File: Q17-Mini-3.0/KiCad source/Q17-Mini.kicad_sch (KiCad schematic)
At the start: 80 parts, among them J1 INPUT, J2-1 SPK+, J2-2 SPK-, J3-1 V+, J3-2 GND, J3-3 V-, Q1 IRF610, Q10 KSA992, Q12 KSC1845, Q13 IRF610, Q14 IRF9610, Q15 FQA46N15, Q16 IXTH48P20P, Q2 KSA992, Q3 KSC1845, Q4 IRF9610, Q5 FQPF7P20, Q6 2SK3564, Q7 LSK170B, Q8 DN2540, Q9 BS250P, U1 OPA1611, U2 NDC7003P

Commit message: Update Q17-Mini.kicad_sch
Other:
- note added: "105mA"
- note added: "95mA"
- note added: "Board consumption per voltage rail without power transistors: 10mA"
- note removed: "35mV with R32 = 10R"
- note removed: "If you have ground loop concerns, you can put R32=0R on one board and R32=10R on the second board. This fixes the problem."
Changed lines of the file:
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@@
 	(title_block
 		(title "Q17-Mini Amplifier")
-		(date "2024-06-29")
-		(rev "2.3.1")
+		(date "2024-07-02")
+		(rev "2.3.2")
 		(company "Principe circuit by Tiberiu Vicol")
 		(comment 1 "Modified by Stef for the Q17-Mini project")
@@
 	(text "max 55V"
 		(exclude_from_sim no)
-		(at 269.24 71.12 0)
+		(at 269.494 68.072 0)
 		(effects
 			(font
@@
 		)
 	)
-	(text "If you have ground loop concerns, you can put R32=0R on one board and R32=10R on the second board. This fixes the problem."
+	(text "Board consumption per voltage rail without power transistors: 10mA"
 		(exclude_from_sim no)
-		(at 85.09 15.24 0)
+		(at 121.412 15.24 0)
 		(effects
 			(font
@@
 		)
 	)
-	(text "35mV with R32 = 10R"
-		(exclude_from_sim no)
-		(at 196.088 81.28 0)
-		(effects
-			(font
-				(size 1.27 1.27)
-				(color 255 3 20 1)
-			)
-			(justify left bottom)
-		)
-	)
 	(text "Q9, U2 : Wilson current mirror (CCS)"
 		(exclude_from_sim no)
@@
 		)
 	)
+	(text "105mA"
+		(exclude_from_sim no)
+		(at 255.27 139.954 0)
+		(effects
+			(font
+				(size 1.27 1.27)
+			)
+			(justify left bottom)
+		)
+	)
 	(text "DC Offset at output < 1mV"
 		(exclude_from_sim no)
@@
 	(text "POWER 50VDC"
 		(exclude_from_sim no)
-		(at 269.24 68.58 0)
+		(at 269.494 65.532 0)
 		(effects
 			(font
@@
 		(effects
 			(font
+				(size 1.27 1.27)
+			)
+			(justify left bottom)
+		)
+	)
+	(text "95mA"
+		(exclude_from_sim no)
+		(at 256.794 26.67 0)
+		(effects
+			(font

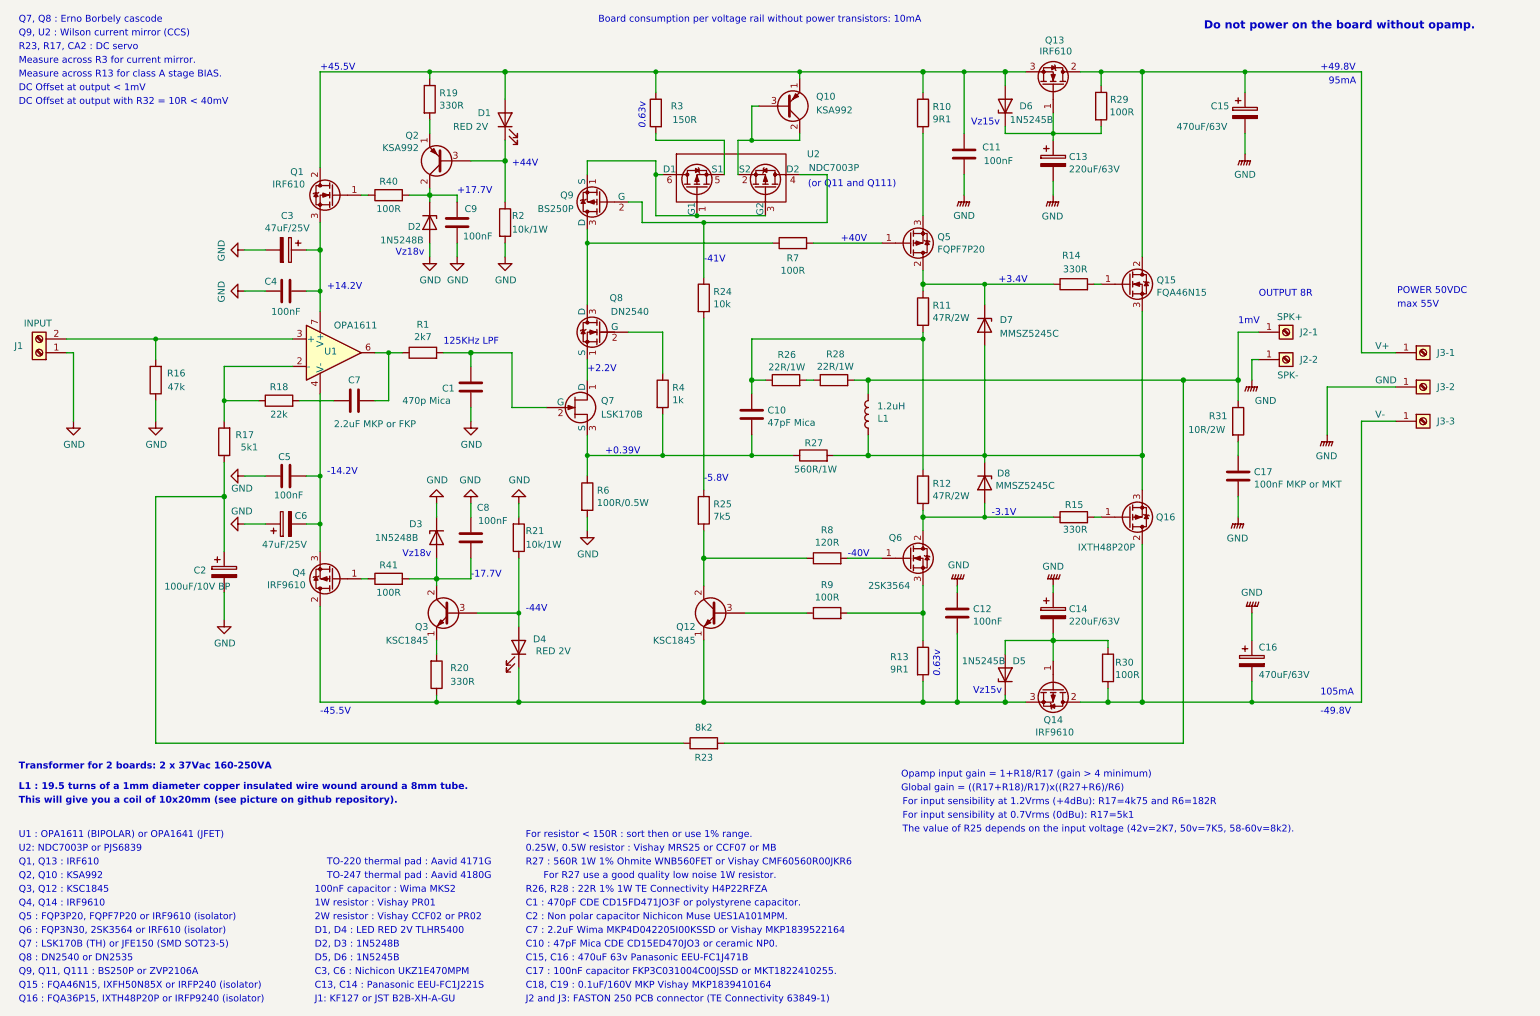
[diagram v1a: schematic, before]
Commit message: Update Q17-Mini 3.0 diagram
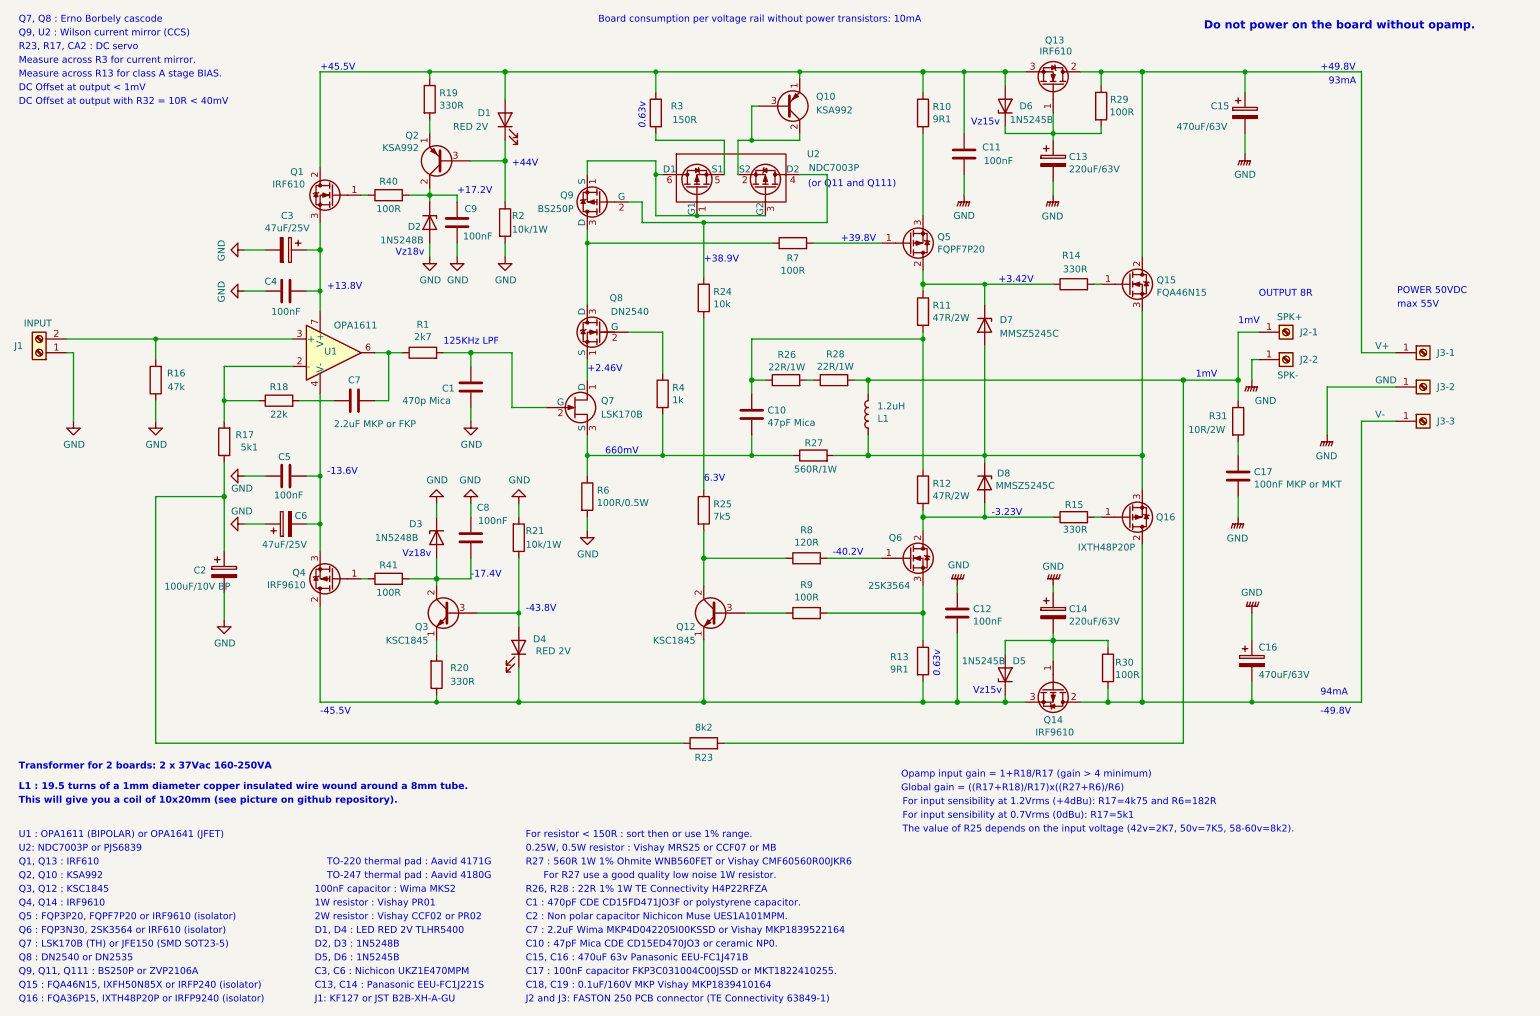
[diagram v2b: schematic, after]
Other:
- note added: "+13.8V"
- note added: "+17.2V"
- note added: "+2.46V"
- note added: "+3.42V"
- note added: "+38.9V"
- note added: "+39.8V"
- note added: "-13.6V"
- note added: "-17.4V"
- note added: "-3.23V"
- note added: "-40.2V"
- note added: "-43.8V"
- note added: "6.3V"
- note added: "660mV"
- note added: "93mA"
- note added: "94mA"
- note removed: "+0.39V"
- note removed: "+14.2V"
- note removed: "+17.7V"
- note removed: "+2.2V"
- note removed: "+3.4V"
- note removed: "+40V"
- note removed: "-14.2V"
- note removed: "-17.7V"
- note removed: "-3.1V"
- note removed: "-40V"
- note removed: "-41V"
- note removed: "-44V"
- note removed: "-5.8V"
- note removed: "105mA"
- note removed: "95mA"
- moved on the sheet: R8, R9
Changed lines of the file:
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@@
 	(title_block
 		(title "Q17-Mini Amplifier")
-		(date "2024-07-02")
+		(date "2024-07-09")
 		(rev "2.3.2")
 		(company "Principe circuit by Tiberiu Vicol")
@@
 	(wire
 		(pts
-			(xy 167.64 114.3) (xy 173.99 114.3)
+			(xy 163.83 114.3) (xy 173.99 114.3)
 		)
 		(stroke
@@
 	(wire
 		(pts
-			(xy 140.97 114.3) (xy 160.02 114.3)
+			(xy 140.97 114.3) (xy 156.21 114.3)
 		)
 		(stroke
@@
 	(wire
 		(pts
-			(xy 167.64 124.46) (xy 181.61 124.46)
+			(xy 163.83 124.46) (xy 181.61 124.46)
 		)
 		(stroke
@@
 	(wire
 		(pts
-			(xy 148.59 124.46) (xy 160.02 124.46)
+			(xy 148.59 124.46) (xy 156.21 124.46)
 		)
 		(stroke
@@
 		)
 	)
-	(text "-44V"
+	(text "-43.8V"
 		(exclude_from_sim no)
 		(at 107.95 124.46 0)
@@
 		)
 	)
-	(text "+2.2V"
+	(text "+2.46V"
 		(exclude_from_sim no)
 		(at 119.38 80.01 0)
@@
 		)
 	)
-	(text "-17.7V"
+	(text "-17.4V"
 		(exclude_from_sim no)
 		(at 97.79 118.11 0)
@@
 		)
 	)
+	(text "1mV"
+		(exclude_from_sim no)
+		(at 232.156 81.026 0)
+		(effects
+			(font
+				(size 1.27 1.27)
+				(color 255 3 20 1)
+			)
+			(justify left bottom)
+		)
+	)
 	(text "1W resistor : Vishay PR01"
 		(exclude_from_sim no)
@@
 		)
 	)
-	(text "-3.1V"
+	(text "-3.23V"
 		(exclude_from_sim no)
 		(at 194.31 106.68 0)
@@
 		)
 	)
-	(text "+0.39V"
+	(text "660mV"
 		(exclude_from_sim no)
 		(at 122.682 95.25 0)
@@
 		)
 	)
-	(text "-5.8V"
+	(text "6.3V"
 		(exclude_from_sim no)
 		(at 140.97 100.33 0)
@@
 		)
 	)
-	(text "+3.4V"
+	(text "+3.42V"
 		(exclude_from_sim no)
 		(at 195.58 63.5 0)
@@
 		)
 	)
-	(text "+14.2V"
+	(text "+13.8V"
 		(exclude_from_sim no)
 		(at 71.12 64.77 0)
@@
 		)
 	)
-	(text "-14.2V"
+	(text "-13.6V"
 		(exclude_from_sim no)
 		(at 71.12 99.06 0)
@@
 		)
 	)
-	(text "+40V"
+	(text "+39.8V"
 		(exclude_from_sim no)
 		(at 166.37 55.88 0)
@@
 		)
 	)
-	(text "105mA"
+	(text "94mA"
 		(exclude_from_sim no)
 		(at 255.27 139.954 0)
@@
 		)
 	)
-	(text "-40V"
+	(text "-40.2V"
 		(exclude_from_sim no)
-		(at 167.64 114.3 0)
+		(at 164.846 114.046 0)
 		(effects
 			(font
@@
 		)
 	)
-	(text "95mA"
+	(text "93mA"
 		(exclude_from_sim no)
 		(at 256.794 26.67 0)
@@
 		)
 	)
-	(text "-41V"
+	(text "+38.9V"
 		(exclude_from_sim no)
 		(at 140.97 59.69 0)
@@
 		)
 	)
-	(text "+17.7V"
+	(text "+17.2V"
 		(exclude_from_sim no)
 		(at 95.25 46.99 0)
@@
 	(symbol
 		(lib_id "Device:R")
-		(at 163.83 124.46 90)
+		(at 160.02 124.46 90)
 		(unit 1)
 		(exclude_from_sim no)
@@
 		(dnp no)
 		(property "Reference" "R9"
-			(at 163.83 119.2338 90)
+			(at 160.02 119.2338 90)
 			(effects
 				(font
@@
 		)
 		(property "Value" "100R"
-			(at 163.83 121.533 90)
+			(at 160.02 121.533 90)
 			(effects
 				(font
@@
 		)
 		(property "Footprint" "Resistor_THT:R_Axial_DIN0207_L6.3mm_D2.5mm_P10.16mm_Horizontal"
-			(at 163.83 126.238 90)
+			(at 160.02 126.238 90)
 			(effects
 				(font
@@
 		)
 		(property "Datasheet" "https://www.vishay.com/doc?28724"
-			(at 163.83 124.46 0)
+			(at 160.02 124.46 0)
 			(effects
 				(font
@@
 		)
 		(property "Description" ""
-			(at 163.83 124.46 0)
+			(at 160.02 124.46 0)
 			(effects
 				(font
@@
 		)
 		(property "Part#" "MRS25000C1000FCT00"
-			(at 163.83 124.46 90)
+			(at 160.02 124.46 90)
 			(effects
 				(font
@@
 		)
 		(property "Mouser" "594-MRS25000C1000FCT"
-			(at 163.83 124.46 90)
+			(at 160.02 124.46 90)
 			(effects
 				(font
@@
 	(symbol
 		(lib_id "Device:R")
-		(at 163.83 114.3 90)
+		(at 160.02 114.3 90)
 		(unit 1)
 		(exclude_from_sim no)
@@
 		(dnp no)
 		(property "Reference" "R8"
-			(at 163.83 109.0738 90)
+			(at 160.02 109.0738 90)
 			(effects
 				(font
@@
 		)
 		(property "Value" "120R"
-			(at 163.83 111.3725 90)
+			(at 160.02 111.3725 90)
 			(effects
 				(font
@@
 		)
 		(property "Footprint" "Resistor_THT:R_Axial_DIN0207_L6.3mm_D2.5mm_P10.16mm_Horizontal"
-			(at 163.83 116.078 90)
+			(at 160.02 116.078 90)
 			(effects
 				(font
@@
 		)
 		(property "Datasheet" "https://www.vishay.com/doc?28724"
-			(at 163.83 114.3 0)
+			(at 160.02 114.3 0)
 			(effects
 				(font
@@
 		)
 		(property "Description" ""
-			(at 163.83 114.3 0)
+			(at 160.02 114.3 0)
 			(effects
 				(font
@@
 		)
 		(property "Part#" "MRS25000C1200FCT00"
-			(at 163.83 114.3 90)
+			(at 160.02 114.3 90)
 			(effects
 				(font
@@
 		)
 		(property "Mouser" "594-MRS25000C1200FCT"
-			(at 163.83 114.3 90)
+			(at 160.02 114.3 90)
 			(effects
 				(font

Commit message: Update diagram for Q17-Mini 3.0
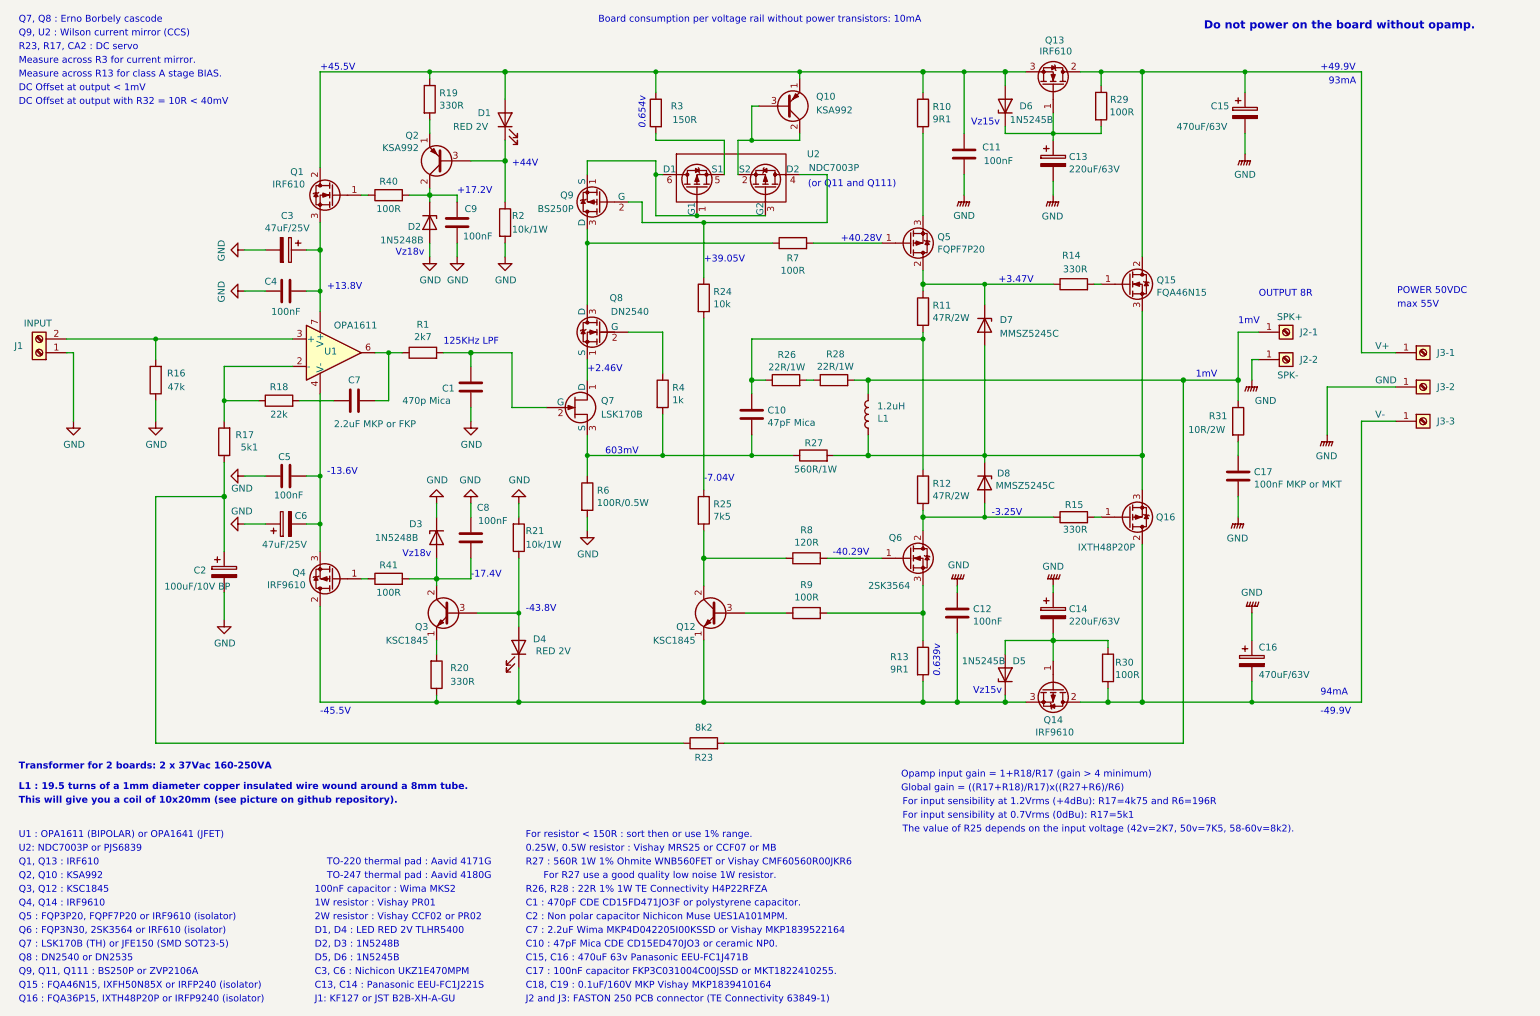
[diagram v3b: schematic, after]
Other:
- note added: "+3.47V"
- note added: "+39.05V"
- note added: "+40.28V"
- note added: "+49.9V"
- note added: "-3.25V"
- note added: "-40.29V"
- note added: "-49.9V"
- note added: "-7.04V"
- note added: "0.639v"
- note added: "0.654v"
- note added: "603mV"
- note added: "For input sensibility at 1.2Vrms (+4dBu): R17=4k75 and R6=196R"
- note removed: "+3.42V"
- note removed: "+38.9V"
- note removed: "+39.8V"
- note removed: "+49.8V"
- note removed: "-3.23V"
- note removed: "-40.2V"
- note removed: "-49.8V"
- note removed: "0.63v"
- note removed: "6.3V"
- note removed: "660mV"
- note removed: "For input sensibility at 1.2Vrms (+4dBu): R17=4k75 and R6=182R"
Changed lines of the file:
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@@
 	(title_block
 		(title "Q17-Mini Amplifier")
-		(date "2024-07-09")
-		(rev "2.3.2")
+		(date "2024-07-15")
+		(rev "2.3.3")
 		(company "Principe circuit by Tiberiu Vicol")
 		(comment 1 "Modified by Stef for the Q17-Mini project")
@@
 		)
 	)
-	(text "-49.8V"
+	(text "-49.9V"
 		(exclude_from_sim no)
 		(at 255.27 143.51 0)
@@
 		)
 	)
-	(text "-3.23V"
+	(text "-3.25V"
 		(exclude_from_sim no)
 		(at 194.31 106.68 0)
@@
 		)
 	)
-	(text "For input sensibility at 1.2Vrms (+4dBu): R17=4k75 and R6=182R"
+	(text "For input sensibility at 1.2Vrms (+4dBu): R17=4k75 and R6=196R"
 		(exclude_from_sim no)
 		(at 177.8 160.274 0)
@@
 		)
 	)
-	(text "660mV"
+	(text "603mV"
 		(exclude_from_sim no)
 		(at 122.682 95.25 0)
@@
 		)
 	)
-	(text "6.3V"
+	(text "-7.04V"
 		(exclude_from_sim no)
 		(at 140.97 100.33 0)
@@
 		)
 	)
-	(text "+3.42V"
+	(text "+3.47V"
 		(exclude_from_sim no)
 		(at 195.58 63.5 0)
@@
 		)
 	)
-	(text "0.63v"
+	(text "0.654v"
 		(exclude_from_sim no)
 		(at 130.302 34.798 90)
@@
 		)
 	)
-	(text "+39.8V"
+	(text "+40.28V"
 		(exclude_from_sim no)
 		(at 166.37 55.88 0)
@@
 		)
 	)
-	(text "-40.2V"
+	(text "-40.29V"
 		(exclude_from_sim no)
 		(at 164.846 114.046 0)
@@
 		)
 	)
-	(text "0.63v"
+	(text "0.639v"
 		(exclude_from_sim no)
 		(at 184.912 136.398 90)
@@
 		)
 	)
-	(text "+38.9V"
+	(text "+39.05V"
 		(exclude_from_sim no)
 		(at 140.97 59.69 0)
@@
 		)
 	)
-	(text "+49.8V"
+	(text "+49.9V"
 		(exclude_from_sim no)
 		(at 255.27 24.13 0)
